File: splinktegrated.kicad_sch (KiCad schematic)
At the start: 53 parts, among them J1 USB_C_Receptacle_USB2.0, J10 Ribbon, J11 Serial, J12 Conn_01x04_Female, J13 Conn_01x02_Female, J14 Cirque, J2 Conn_01x04_Female, J3 Conn_01x04_Female, J4 Conn_01x04_Female, J5 Conn_01x02, J6 Serial, J7 trackball, J8 Ribbon, J9 RGB, SW1 SW_SPST, SW2 SW_SPST, U1 RP2040, U2 USBLC6-2P6, U3 XC6210B332MR-G, U4 USBLC6-2P6, U5 W25Q128JVS, Y1 Crystal_GND24

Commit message: routing
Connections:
- net +3V3: no longer J14.1 (Pin_1)
- net GND: no longer J14.13 (Pin_13)
- net rgb_r: no longer J14.14 (Pin_14)
- no-connect marks 18 -> 21
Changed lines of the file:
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@@
   (no_connect (at 182.88 104.14))
   (no_connect (at 182.88 86.36))
+  (no_connect (at 391.16 62.23))
   (no_connect (at 182.88 88.9))
   (no_connect (at 182.88 91.44))
@@
   (no_connect (at -88.9 63.5))
   (no_connect (at 379.73 135.89))
+  (no_connect (at 391.16 64.77))
   (no_connect (at 182.88 63.5))
   (no_connect (at 182.88 66.04))
@@
   (no_connect (at 127 120.65))
   (no_connect (at 379.73 140.97))
+  (no_connect (at 391.16 67.31))
   (polyline (pts (xy 209.55 96.52) (xy 279.4 96.52))
     (stroke (width 0) (type default))
@@
     (effects (font (size 1.27 1.27)) (justify right))
     (property "Intersheetrefs" "${INTERSHEET_REFS}" (at 323.85 -16.51 0)
-      (effects (font (size 1.27 1.27)) hide)
-    )
-  )
-  (global_label "rgb_r" (shape input) (at 391.16 67.31 180)
-    (effects (font (size 1.27 1.27)) (justify right))
-    (property "Intersheetrefs" "${INTERSHEET_REFS}" (at 247.015 -9.525 0)
       (effects (font (size 1.27 1.27)) hide)
     )
@@
     )
   )
-  (symbol (lib_id "power:+3.3V") (at 391.16 62.23 90) (unit 1)
-    (in_bom yes) (on_board yes) (dnp no)
-    (property "Reference" "#PWR032" (at 394.97 62.23 0)
-      (effects (font (size 1.27 1.27)) hide)
-    )
-    (property "Value" "+3.3V" (at 387.35 62.23 0)
-      (effects (font (size 1.27 1.27)))
-    )
-    (property "Footprint" "" (at 391.16 62.23 0)
-      (effects (font (size 1.27 1.27)) hide)
-    )
-    (property "Datasheet" "" (at 391.16 62.23 0)
-      (effects (font (size 1.27 1.27)) hide)
-    )
-    (pin "1")
-    (instances
-      (project "splinktegrated"
-        (path "/7353e96a-343a-4876-b497-b1d205a14d97"
-          (reference "#PWR032") (unit 1)
-        )
-      )
-    )
-  )
   (symbol (lib_id "Connector:Conn_01x05_Female") (at 358.14 27.94 0) (unit 1)
     (in_bom no) (on_board yes) (dnp no)
@@
         )
       )
-    )
-  )
-  (symbol (lib_id "power:GND") (at 391.16 64.77 270) (unit 1)
-    (in_bom yes) (on_board yes) (dnp no)
-    (property "Reference" "#PWR034" (at 384.81 64.77 0)
-      (effects (font (size 1.27 1.27)) hide)
-    )
-    (property "Value" "GND" (at 384.1751 64.614 90)
-      (effects (font (size 1.27 1.27)) (justify left))
-    )
-    (property "Footprint" "" (at 391.16 64.77 0)
-      (effects (font (size 1.27 1.27)) hide)
-    )
-    (property "Datasheet" "" (at 391.16 64.77 0)
-      (effects (font (size 1.27 1.27)) hide)
-    )
-    (pin "1")
-    (instances
-      (project "splinktegrated"
-        (path "/7353e96a-343a-4876-b497-b1d205a14d97"
-          (reference "#PWR034") (unit 1)
-        )
-      )

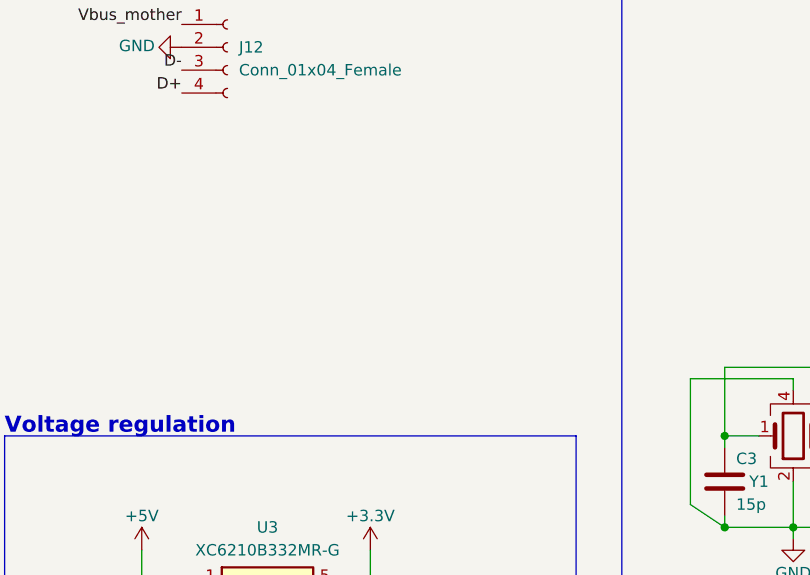
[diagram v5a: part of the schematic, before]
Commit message: screw holes
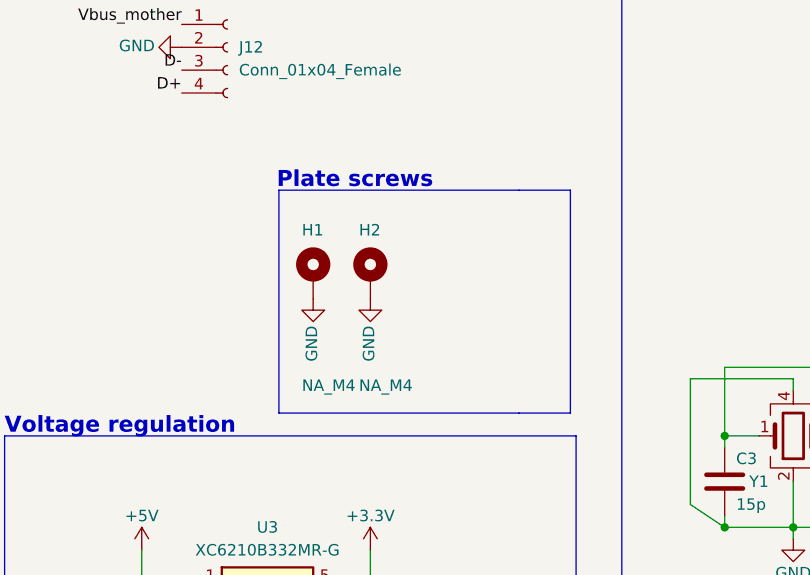
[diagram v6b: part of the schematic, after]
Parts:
- added H1, H2: NA_M4, Library:MountingHole_4mm_Pad_Via, symbol Mechanical:MountingHole_Pad
- J2, J3: footprint drawings:PinHeader_1x04_P2.54mm_Vertical -> Library:PinHeader_1x04_P2.54mm_Vertical_USB
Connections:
- net GND: now also H1.1, H2.1
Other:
- note added: "Plate screws"
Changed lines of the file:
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@@
     (stroke (width 0) (type default))
   )
+  (polyline (pts (xy 80.645 69.215) (xy 80.645 93.98))
+    (stroke (width 0) (type default))
+  )
   (wire (pts (xy 243.84 142.24) (xy 243.84 144.78))
     (stroke (width 0) (type default))
@@
     (stroke (width 0) (type default))
   )
+  (polyline (pts (xy 74.93 93.98) (xy 48.26 93.98))
+    (stroke (width 0) (type default))
+  )
   (wire (pts (xy -88.9 33.02) (xy -86.36 33.02))
     (stroke (width 0) (type default))
@@
     (stroke (width 0) (type default))
   )
+  (polyline (pts (xy 48.26 69.215) (xy 48.26 93.98))
+    (stroke (width 0) (type default))
+  )
   (wire (pts (xy 91.44 184.15) (xy 91.44 186.69))
     (stroke (width 0) (type default))
@@
     (stroke (width 0) (type default))
   )
+  (polyline (pts (xy 48.26 69.215) (xy 74.93 69.215))
+    (stroke (width 0) (type default))
+  )
   (wire (pts (xy -68.58 38.1) (xy -68.58 40.64))
     (stroke (width 0) (type default))
@@
     (stroke (width 0) (type default))
   )
+  (polyline (pts (xy 74.93 69.215) (xy 80.645 69.215))
+    (stroke (width 0) (type default))
+  )
   (wire (pts (xy 40.005 162.56) (xy 40.005 163.83))
     (stroke (width 0) (type default))
@@
     (stroke (width 0) (type default))
   )
+  (polyline (pts (xy 80.645 93.98) (xy 74.93 93.98))
+    (stroke (width 0) (type default))
+  )
   (wire (pts (xy 46.99 127) (xy 58.42 127))
     (stroke (width 0) (type default))
@@
     (effects (font (size 1.778 1.778) (thickness 0.3556) bold) (justify left bottom))
   )
+  (text "Plate screws" (at 65.405 69.215 0)
+    (effects (font (size 1.778 1.778) (thickness 0.3556) bold) (justify right bottom))
+  )
   (text "Flash memory" (at 209.55 104.14 0)
     (effects (font (size 1.778 1.778) (thickness 0.3556) bold) (justify left bottom))
@@
     )
   )
+  (symbol (lib_id "Mechanical:MountingHole_Pad") (at 58.42 78.74 0) (unit 1)
+    (in_bom yes) (on_board yes) (dnp no)
+    (property "Reference" "H2" (at 57.15 73.66 0)
+      (effects (font (size 1.27 1.27)) (justify left))
+    )
+    (property "Value" "NA_M4" (at 57.15 90.932 0)
+      (effects (font (size 1.27 1.27)) (justify left))
+    )
+    (property "Footprint" "Library:MountingHole_4mm_Pad_Via" (at 58.42 78.74 0)
+      (effects (font (size 1.27 1.27)) hide)
+    )
+    (property "Datasheet" "~" (at 58.42 78.74 0)
+      (effects (font (size 1.27 1.27)) hide)
+    )
+    (pin "1")
+    (instances
+      (project "splinktegrated"
+        (path "/7353e96a-343a-4876-b497-b1d205a14d97"
+          (reference "H2") (unit 1)
+        )
+      )
+    )
+  )
   (symbol (lib_id "Switch:SW_SPST") (at 48.895 214.63 0) (unit 1)
     (in_bom no) (on_board yes) (dnp no)
@@
       (effects (font (size 1.27 1.27)) (justify left))
     )
-    (property "Footprint" "drawings:PinHeader_1x04_P2.54mm_Vertical" (at -62.23 69.215 0)
+    (property "Footprint" "Library:PinHeader_1x04_P2.54mm_Vertical_USB" (at -62.23 69.215 0)
       (effects (font (size 1.27 1.27)) hide)
     )
@@
     )
   )
+  (symbol (lib_id "power:GND") (at 58.42 81.28 0) (unit 1)
+    (in_bom yes) (on_board yes) (dnp no)
+    (property "Reference" "#PWR034" (at 58.42 87.63 0)
+      (effects (font (size 1.27 1.27)) hide)
+    )
+    (property "Value" "GND" (at 58.264 88.2649 90)
+      (effects (font (size 1.27 1.27)) (justify left))
+    )
+    (property "Footprint" "" (at 58.42 81.28 0)
+      (effects (font (size 1.27 1.27)) hide)
+    )
+    (property "Datasheet" "" (at 58.42 81.28 0)
+      (effects (font (size 1.27 1.27)) hide)
+    )
+    (pin "1")
+    (instances
+      (project "splinktegrated"
+        (path "/7353e96a-343a-4876-b497-b1d205a14d97"
+          (reference "#PWR034") (unit 1)
+        )
+      )
+    )
+  )
   (symbol (lib_id "Device:R") (at 24.765 181.61 180) (unit 1)
     (in_bom yes) (on_board yes) (dnp no)
@@
       (effects (font (size 1.27 1.27)) (justify left))
     )
-    (property "Footprint" "drawings:PinHeader_1x04_P2.54mm_Vertical" (at -61.595 82.55 0)
+    (property "Footprint" "Library:PinHeader_1x04_P2.54mm_Vertical_USB" (at -61.595 82.55 0)
       (effects (font (size 1.27 1.27)) hide)
     )
@@
     )
   )
+  (symbol (lib_id "Mechanical:MountingHole_Pad") (at 52.07 78.74 0) (unit 1)
+    (in_bom yes) (on_board yes) (dnp no)
+    (property "Reference" "H1" (at 50.8 73.66 0)
+      (effects (font (size 1.27 1.27)) (justify left))
+    )
+    (property "Value" "NA_M4" (at 50.8 90.932 0)
+      (effects (font (size 1.27 1.27)) (justify left))
+    )
+    (property "Footprint" "Library:MountingHole_4mm_Pad_Via" (at 52.07 78.74 0)
+      (effects (font (size 1.27 1.27)) hide)
+    )
+    (property "Datasheet" "~" (at 52.07 78.74 0)
+      (effects (font (size 1.27 1.27)) hide)
+    )
+    (pin "1")
+    (instances
+      (project "splinktegrated"
+        (path "/7353e96a-343a-4876-b497-b1d205a14d97"
+          (reference "H1") (unit 1)
+        )
+      )
+    )
+  )
   (symbol (lib_id "power:+3.3V") (at 171.45 36.83 0) (unit 1)
     (in_bom yes) (on_board yes) (dnp no)
@@
         )
       )
+    )
+  )
+  (symbol (lib_id "power:GND") (at 52.07 81.28 0) (unit 1)
+    (in_bom yes) (on_board yes) (dnp no)
+    (property "Reference" "#PWR032" (at 52.07 87.63 0)
+      (effects (font (size 1.27 1.27)) hide)
+    )
+    (property "Value" "GND" (at 51.914 88.2649 90)
+      (effects (font (size 1.27 1.27)) (justify left))
+    )
+    (property "Footprint" "" (at 52.07 81.28 0)
+      (effects (font (size 1.27 1.27)) hide)
+    )
+    (property "Datasheet" "" (at 52.07 81.28 0)
+      (effects (font (size 1.27 1.27)) hide)
+    )
+    (pin "1")
+    (instances
+      (project "splinktegrated"
+        (path "/7353e96a-343a-4876-b497-b1d205a14d97"
+          (reference "#PWR032") (unit 1)
+        )
+      )

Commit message: assembly / non assembly labels
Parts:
- J10, J8: value Ribbon -> NA_Ribbon
- J11: value Serial -> NA_Serial
- J12, J2, J3, J4: value Conn_01x04_Female -> NA_Conn_01x04_Female
- J7: value trackball -> NA_trackball
- J9: value RGB -> NA_RGB
- NA_JP1: renamed from JP1; value Jumper_2_Open -> NA_Jumper_2_Open
- NA_JP2: renamed from JP2; value Jumper_2_Open -> NA_Jumper_2_Open
- SW1, SW2: value SW_SPST -> NA_SW_SPST
- renumbered J6 to NA_J6
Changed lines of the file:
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@@
       (effects (font (size 1.27 1.27)) (justify left))
     )
-    (property "Value" "Ribbon" (at 349.25 38.1 0)
+    (property "Value" "NA_Ribbon" (at 349.25 38.1 0)
       (effects (font (size 1.27 1.27)) (justify left))
     )
@@
       (effects (font (size 1.27 1.27)))
     )
-    (property "Value" "SW_SPST" (at 48.895 210.82 0)
+    (property "Value" "NA_SW_SPST" (at 48.895 210.82 0)
       (effects (font (size 1.27 1.27)))
     )
@@
   (symbol (lib_id "Jumper:Jumper_2_Open") (at 326.39 99.06 0) (unit 1)
     (in_bom no) (on_board yes) (dnp no)
-    (property "Reference" "JP1" (at 320.04 109.22 0)
-      (effects (font (size 1.27 1.27)))
-    )
-    (property "Value" "Jumper_2_Open" (at 326.39 105.41 0)
+    (property "Reference" "NA_JP1" (at 320.04 109.22 0)
+      (effects (font (size 1.27 1.27)))
+    )
+    (property "Value" "NA_Jumper_2_Open" (at 326.39 105.41 0)
       (effects (font (size 1.27 1.27)))
     )
@@
       (project "splinktegrated"
         (path "/7353e96a-343a-4876-b497-b1d205a14d97"
-          (reference "JP1") (unit 1)
+          (reference "NA_JP1") (unit 1)
         )
       )
@@
   (symbol (lib_id "Connector:Conn_01x04_Female") (at -62.23 69.215 0) (unit 1)
     (in_bom no) (on_board yes) (dnp no) (fields_autoplaced)
-    (property "Reference" "J2" (at -60.96 69.2149 0)
-      (effects (font (size 1.27 1.27)) (justify left))
-    )
-    (property "Value" "Conn_01x04_Female" (at -60.96 71.7549 0)
+    (property "Reference" "J2" (at -59.69 69.85 0)
+      (effects (font (size 1.27 1.27)) (justify left))
+    )
+    (property "Value" "NA_Conn_01x04_Female" (at -59.69 72.39 0)
       (effects (font (size 1.27 1.27)) (justify left))
     )
@@
   (symbol (lib_id "Jumper:Jumper_2_Open") (at 332.74 137.16 0) (unit 1)
     (in_bom no) (on_board yes) (dnp no)
-    (property "Reference" "JP2" (at 332.74 144.78 0)
-      (effects (font (size 1.27 1.27)))
-    )
-    (property "Value" "Jumper_2_Open" (at 332.74 140.97 0)
+    (property "Reference" "NA_JP2" (at 332.74 144.78 0)
+      (effects (font (size 1.27 1.27)))
+    )
+    (property "Value" "NA_Jumper_2_Open" (at 332.74 140.97 0)
       (effects (font (size 1.27 1.27)))
     )
@@
       (project "splinktegrated"
         (path "/7353e96a-343a-4876-b497-b1d205a14d97"
-          (reference "JP2") (unit 1)
+          (reference "NA_JP2") (unit 1)
         )
       )
@@
       (effects (font (size 1.27 1.27)))
     )
-    (property "Value" "SW_SPST" (at 49.53 201.295 0)
+    (property "Value" "NA_SW_SPST" (at 49.53 201.295 0)
       (effects (font (size 1.27 1.27)))
     )
@@
       (effects (font (size 1.27 1.27)) (justify left))
     )
-    (property "Value" "RGB" (at 333.248 38.608 0)
+    (property "Value" "NA_RGB" (at 333.248 38.608 0)
       (effects (font (size 1.27 1.27)) (justify left))
     )
@@
   (symbol (lib_id "Connector:Conn_01x04_Female") (at 41.91 40.005 0) (unit 1)
     (in_bom no) (on_board yes) (dnp no) (fields_autoplaced)
-    (property "Reference" "J4" (at 43.18 40.0049 0)
-      (effects (font (size 1.27 1.27)) (justify left))
-    )
-    (property "Value" "Conn_01x04_Female" (at 43.18 42.5449 0)
+    (property "Reference" "J4" (at 43.18 40.64 0)
+      (effects (font (size 1.27 1.27)) (justify left))
+    )
+    (property "Value" "NA_Conn_01x04_Female" (at 43.18 43.18 0)
       (effects (font (size 1.27 1.27)) (justify left))
     )
@@
       (effects (font (size 1.27 1.27)) (justify left))
     )
-    (property "Value" "Ribbon" (at 310.515 69.215 0)
+    (property "Value" "NA_Ribbon" (at 310.515 69.215 0)
       (effects (font (size 1.27 1.27)) (justify left))
     )
@@
   (symbol (lib_id "Connector:Conn_01x04_Female") (at -61.595 82.55 0) (unit 1)
     (in_bom no) (on_board yes) (dnp no) (fields_autoplaced)
-    (property "Reference" "J3" (at -60.325 82.5499 0)
-      (effects (font (size 1.27 1.27)) (justify left))
-    )
-    (property "Value" "Conn_01x04_Female" (at -60.325 85.0899 0)
+    (property "Reference" "J3" (at -58.42 83.185 0)
+      (effects (font (size 1.27 1.27)) (justify left))
+    )
+    (property "Value" "NA_Conn_01x04_Female" (at -58.42 85.725 0)
       (effects (font (size 1.27 1.27)) (justify left))
     )
@@
       (effects (font (size 1.27 1.27)))
     )
-    (property "Value" "Serial" (at 322.58 145.415 0)
+    (property "Value" "NA_Serial" (at 322.58 145.415 0)
       (effects (font (size 1.27 1.27)))
     )
@@
       (effects (font (size 1.27 1.27)) (justify left))
     )
-    (property "Value" "trackball" (at 311.15 38.1 0)
+    (property "Value" "NA_trackball" (at 311.15 38.1 0)
       (effects (font (size 1.27 1.27)) (justify left))
     )
@@
   (symbol (lib_id "Connector:AudioJack4") (at 316.23 93.98 0) (unit 1)
     (in_bom no) (on_board yes) (dnp no)
-    (property "Reference" "J6" (at 315.087 85.8582 0)
+    (property "Reference" "NA_J6" (at 315.087 85.8582 0)
       (effects (font (size 1.27 1.27)))
     )
@@
       (project "splinktegrated"
         (path "/7353e96a-343a-4876-b497-b1d205a14d97"
-          (reference "J6") (unit 1)
+          (reference "NA_J6") (unit 1)
         )
       )
@@
   (symbol (lib_id "Connector:Conn_01x04_Female") (at 42.545 53.34 0) (unit 1)
     (in_bom no) (on_board yes) (dnp no) (fields_autoplaced)
-    (property "Reference" "J12" (at 43.815 53.3399 0)
-      (effects (font (size 1.27 1.27)) (justify left))
-    )
-    (property "Value" "Conn_01x04_Female" (at 43.815 55.8799 0)
-      (effects (font (size 1.27 1.27)) (justify left))
-    )
+    (property "Reference" "J12" (at 44.45 53.975 0)
+      (effects (font (size 1.27 1.27)) (justify left))
+    )
+    (property "Value" "NA_Conn_01x04_Female" (at 44.45 56.515 0)
+      (effects (font (size 1.27 1.27)) (justify left))
+    )

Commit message: routin
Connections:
- net col1_l: now also J14.5 (Pin_5); no longer J14.3 (Pin_3)
- net col3_l: now also J14.2 (Pin_2); no longer J14.6 (Pin_6)
- net col4_l: now also J14.9 (Pin_9); no longer J14.10 (Pin_10)
- net col5_l: now also J14.10 (Pin_10); no longer J14.9 (Pin_9)
- net col6_l: now also J14.11 (Pin_11); no longer J14.8 (Pin_8)
- net row1_l: now also J14.3 (Pin_3); no longer J14.5 (Pin_5)
- net row2_l: now also J14.6 (Pin_6); no longer J14.2 (Pin_2)
- net row3_l: now also J14.8 (Pin_8); no longer J14.11 (Pin_11)
- net row4_l: now also J14.7 (Pin_7); no longer J14.12 (Pin_12)
- net row5_l: now also J14.12 (Pin_12); no longer J14.7 (Pin_7)
